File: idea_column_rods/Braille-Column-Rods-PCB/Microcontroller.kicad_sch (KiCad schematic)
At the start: 12 parts, among them J2 Conn_01x02, J3 Conn_01x02, J4 Conn_01x08, SW1 SW_Push, SW2 SW_Push, U3 RP2040-Zero

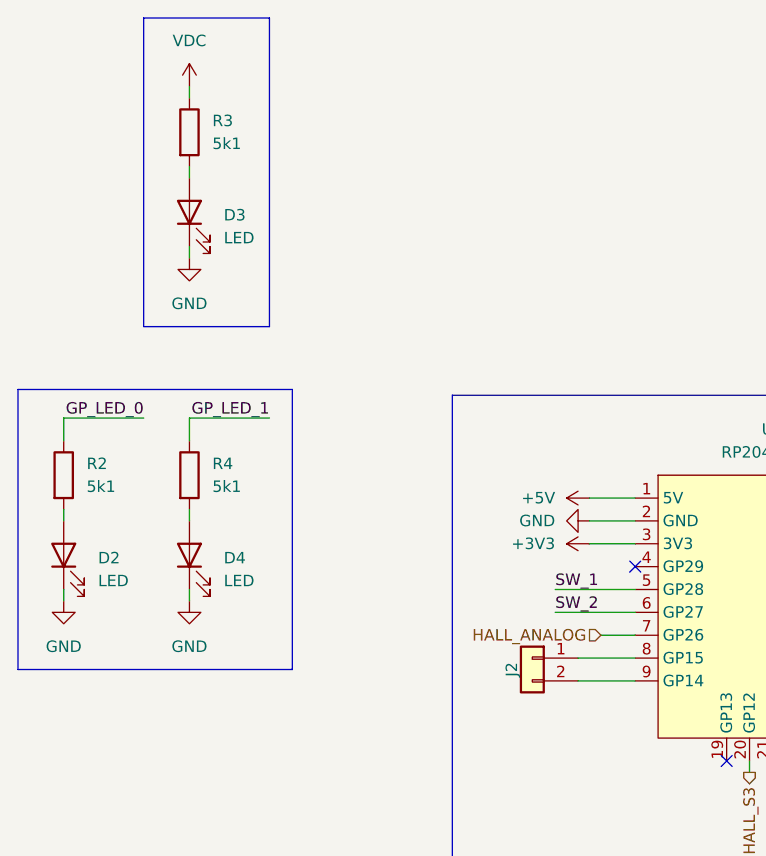
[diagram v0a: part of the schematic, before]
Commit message: Create PCB and CAD for Type 4 Rev 1 rod cams (#13)
* WIP: Rods PCB placement

* WIP: Place the housing and motor X

* WIP: Position everything

* WIP: Update tight placement of DC motor

* WIP: Layout and route the stepper driver

* WIP: Motor layout is good

* WIP: Manual routing and silkscreens

* Comments

* Big routing

* Clean up DRC (mostly footprints)

* Fix spacing issue on top

* Fix spacing issues on bottom

* Create render of 6mm motor, add to PCB

* WIP: Get cams good

* WIP: Reorder the cam bushing and hall sensor

* Finish and tag release

* Complete type 4 rev 1

* Create dc_motor_clamp cad
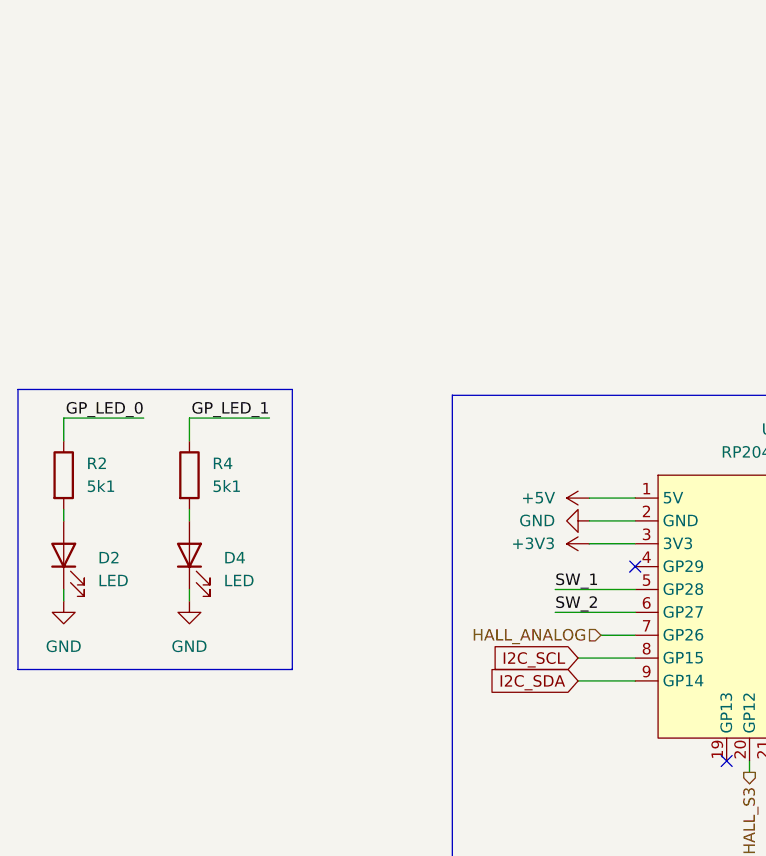
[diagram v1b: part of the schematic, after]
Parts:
- removed D3: LED, LED_SMD:LED_0603_1608Metric_Pad1.05x0.95mm_HandSolder, symbol Device:LED
- removed J2: Conn_01x02, Connector_PinHeader_2.54mm:PinHeader_1x02_P2.54mm_Vertical, symbol Connector_Generic:Conn_01x02
- removed R3: 5k1, Resistor_SMD:R_0603_1608Metric_Pad0.98x0.95mm_HandSolder, symbol Device:R
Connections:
- net I2C_SCL: now reaches U3.8 (GP15)
- net I2C_SDA: now reaches U3.9 (GP14)
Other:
- title: (none) -> Braille Cam Rod Prototype (Type 4)
